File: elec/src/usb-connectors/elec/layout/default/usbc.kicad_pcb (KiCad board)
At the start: 2 copper layers, 3 parts

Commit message: fixed maybe
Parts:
- moved R2 77.0 mm to (178.0, 122.3), turned to 0 degrees
- moved R1 76.6 mm to (178.0, 119.6), turned to 0 degrees
- moved U1 70.2 mm to (173.5, 120.6), turned to -90 degrees
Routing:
- net cc2: track 1.65 -> 0.00 mm
- net cc1: track 1.60 -> 0.00 mm

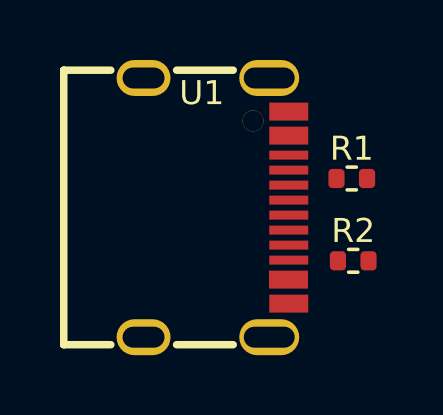
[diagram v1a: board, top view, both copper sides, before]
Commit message: updated usb package
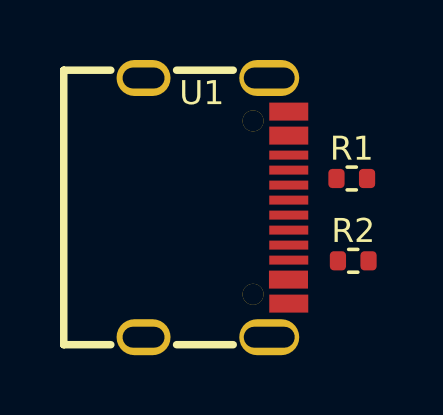
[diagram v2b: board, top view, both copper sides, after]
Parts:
- added ?: , , F.Cu at (174.7, 123.5)
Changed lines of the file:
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@@
 	(net 7 "cc2")
 	(net 8 "sub1")
+	(footprint ""
+		(layer "F.Cu")
+		(at 174.71 123.46)
+		(property "Reference" ""
+			(at 0 0 0)
+			(layer "F.SilkS")
+			(effects
+				(font
+					(size 1.27 1.27)
+					(thickness 0.15)
+				)
+			)
+		)
+		(property "Value" ""
+			(at 0 0 0)
+			(layer "F.Fab")
+			(effects
+				(font
+					(size 1.27 1.27)
+					(thickness 0.15)
+				)
+			)
+		)
+		(property "Footprint" ""
+			(at 0 0 0)
+			(layer "F.Fab")
+			(hide yes)
+			(effects
+				(font
+					(size 1.27 1.27)
+					(thickness 0.15)
+				)
+			)
+		)
+		(property "Datasheet" ""
+			(at 0 0 0)
+			(layer "F.Fab")
+			(hide yes)
+			(effects
+				(font
+					(size 1.27 1.27)
+					(thickness 0.15)
+				)
+			)
+		)
+		(property "Description" ""
+			(at 0 0 0)
+			(layer "F.Fab")
+			(hide yes)
+			(effects
+				(font
+					(size 1.27 1.27)
+					(thickness 0.15)
+				)
+			)
+		)
+		(pad "" thru_hole circle
+			(at 0 0 270)
+			(size 0.7 0.7)
+			(drill 0.7)
+			(layers "*.Cu" "*.Mask")
+			(remove_unused_layers no)
+		)
+	)
 	(footprint "lib:USB-C-SMD_KH-TYPE-C-16P"
 		(layer "F.Cu")
